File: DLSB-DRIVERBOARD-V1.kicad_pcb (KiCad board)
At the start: 2 copper layers, 12 x 28 mm, 16 parts, among them J1 HEAD-I01-X-PI2X03-SM-H2X3SM, J2 HEAD-I01-X-PI2X03-SM-H2X3SM, J3 HEAD-JSTSH-X-PI04-RS-HSH04RS, J4 HEAD-I01-X-PI01-01-HP01, Q1 TRNN-SO23-X-KS8050-01-TRNN-SO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, Q2 MOSN-T252-X-K4184-01-MN252418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, U1 MCUU-SC14-84-ATTINY-01-MCAT84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, U2 VREG-SO223-X-KLD1117-V33D-VR1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, Y1 XTAL-5032-X-MZ16-01-XTAL5032-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

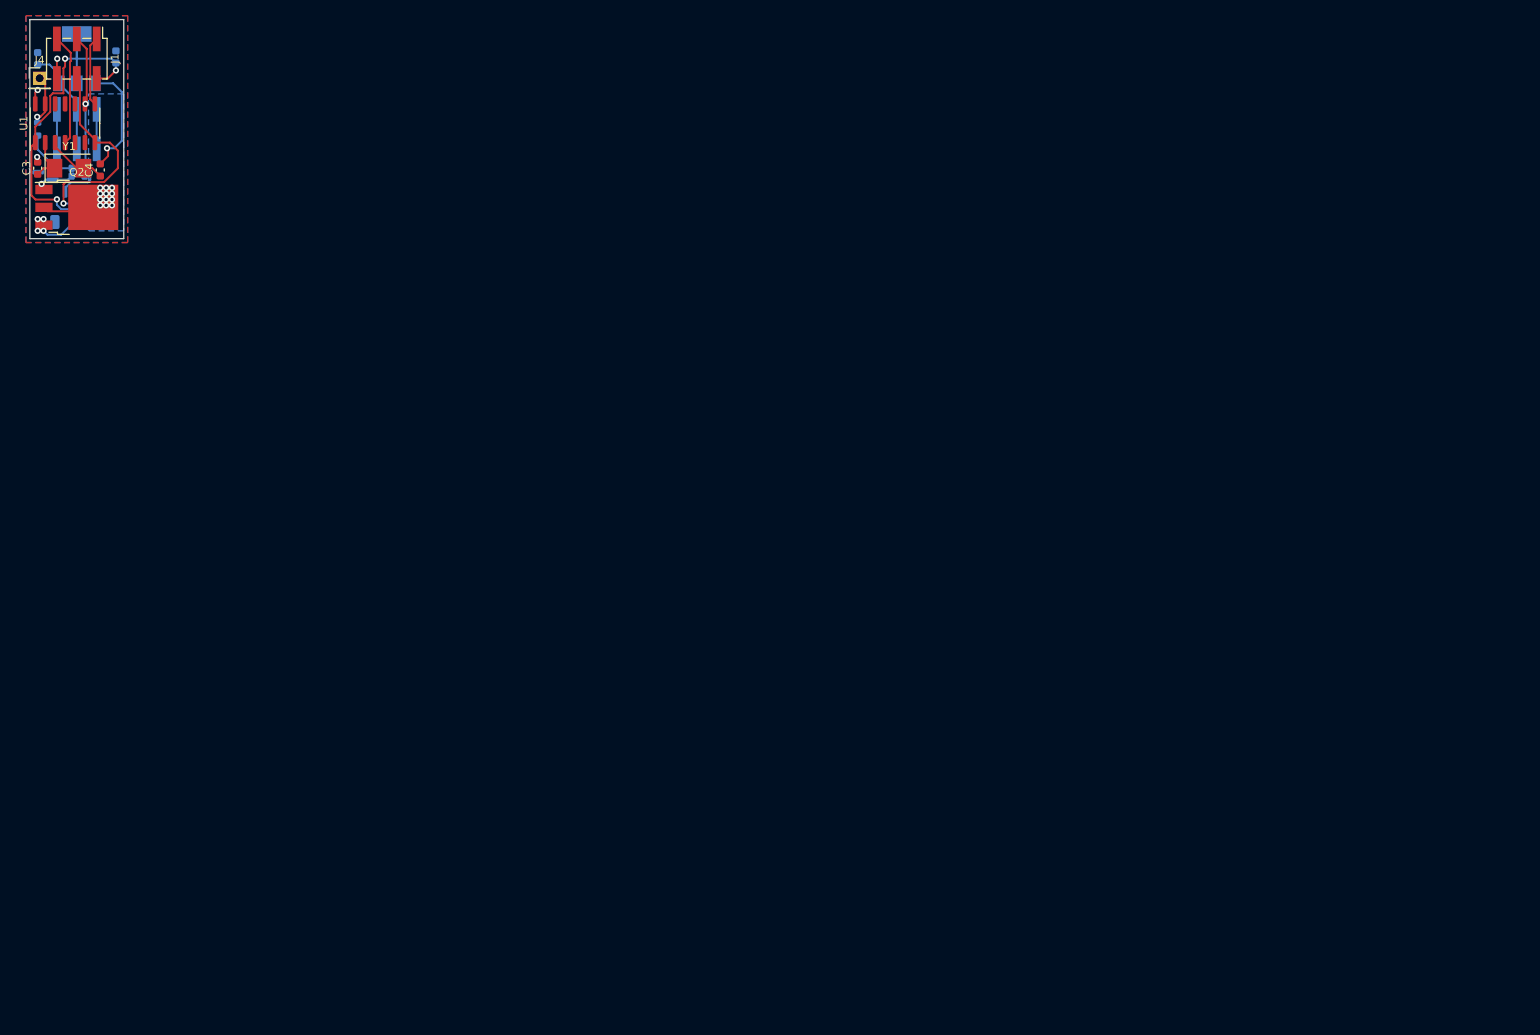
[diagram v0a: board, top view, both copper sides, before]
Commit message: moved board to center of page.
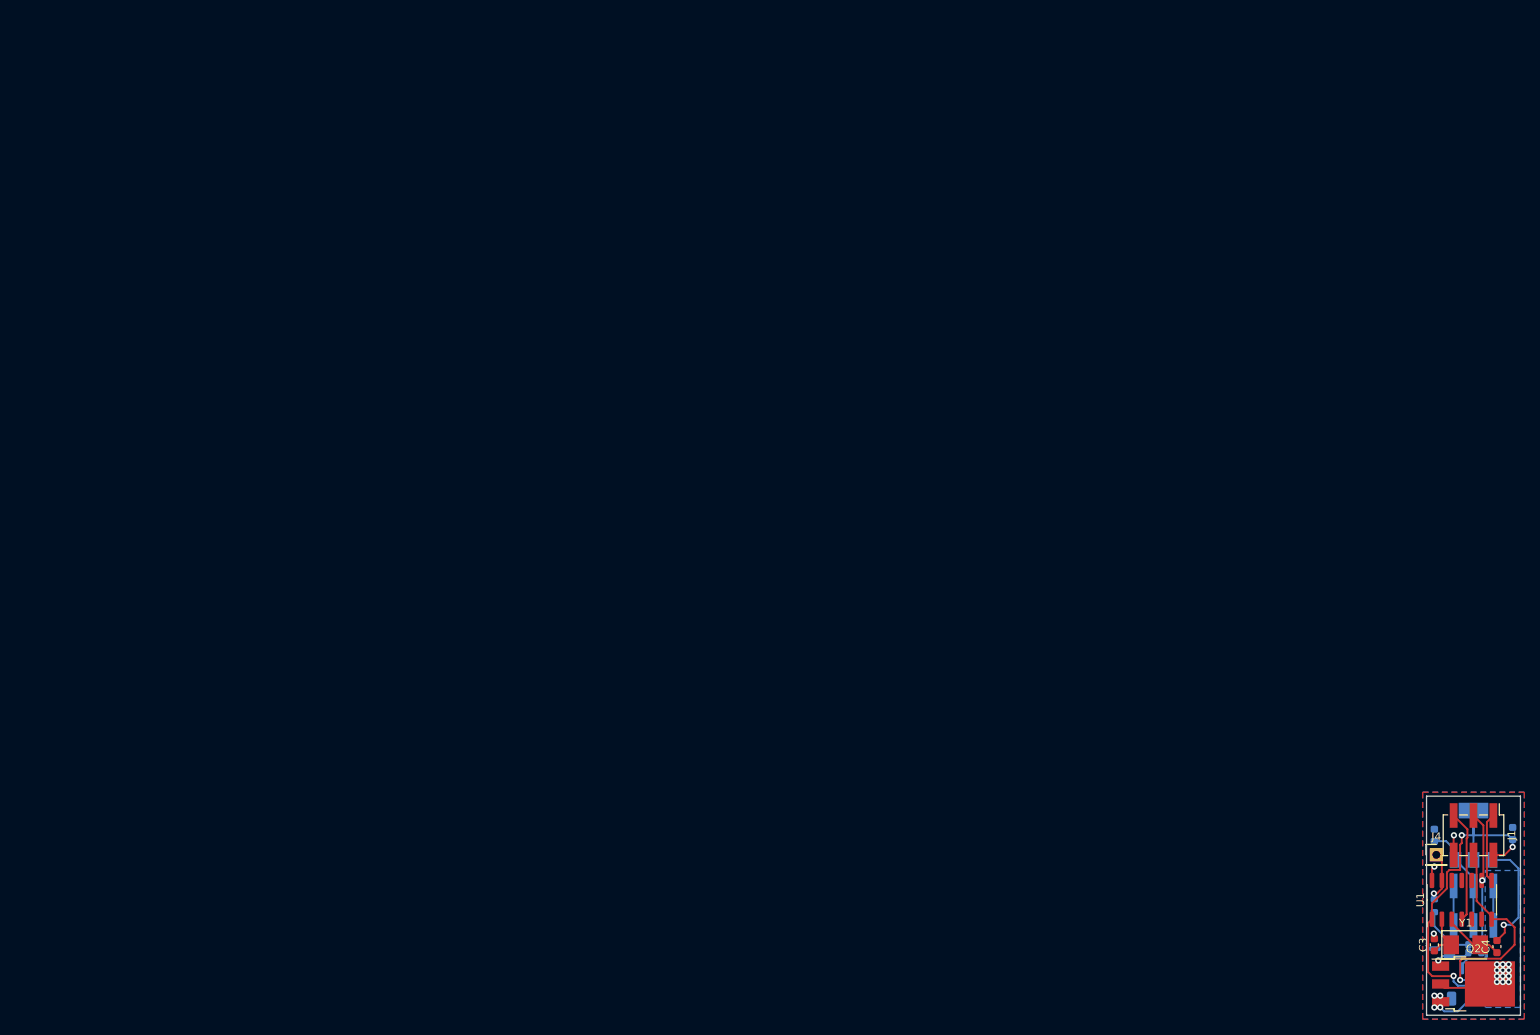
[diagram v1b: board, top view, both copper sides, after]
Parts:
- moved C1 204.2 mm to (173.5, 90.2)
- moved C2 204.2 mm to (183.5, 90.0)
- moved C3 204.2 mm to (173.5, 104.2)
- moved C4 204.2 mm to (181.5, 104.5)
- moved J1 204.2 mm to (178.5, 90.2)
- moved J2 204.2 mm to (178.5, 99.2)
- moved J3 204.2 mm to (178.5, 109.2)
- moved J4 204.2 mm to (173.8, 92.8)
- moved Q1 204.2 mm to (174.5, 104.8)
- moved Q2 204.2 mm to (178.5, 109.2)
- moved R1 204.2 mm to (173.5, 99.2)
- moved R2 204.2 mm to (178.7, 104.2)
- moved R3 204.2 mm to (178.7, 105.2)
- moved U1 204.2 mm to (177.0, 98.5)
- moved U2 204.2 mm to (178.5, 90.2)
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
